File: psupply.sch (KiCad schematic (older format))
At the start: 23 parts, among them U401 LM7815_TO220, U402 LM7915_TO220

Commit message: The board shall now support single channel only.
Signed-off-by: Nenad Radulovic <nenad.radulovic@seavus.com>
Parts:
- removed C402: 10u, Capacitor_THT:CP_Radial_D5.0mm_P2.00mm, symbol CP1
- removed C406, C408: 470n, Capacitor_THT:C_Rect_L9.0mm_W3.6mm_P7.50mm_MKT, symbol C
- removed C407: 10n, Capacitor_THT:C_Rect_L9.0mm_W3.4mm_P7.50mm_MKT, symbol C
- removed C410: 10m, Capacitor_THT:CP_Radial_D35.0mm_P10.00mm_SnapIn, symbol CP1
- removed D401, D402: 1N4007, Diode_THT:D_DO-41_SOD81_P10.16mm_Horizontal, symbol 1N4007
- removed D403: GBU1510, Diode_THT:Diode_Bridge_Vishay_GBU, symbol GBU4A
- removed R405: 1, Resistor_THT:R_Axial_DIN0309_L9.0mm_D3.2mm_P12.70mm_Horizontal, symbol R
- removed R406: 5k1, Resistor_THT:R_Axial_DIN0411_L9.9mm_D3.6mm_P12.70mm_Horizontal, symbol R
- removed U401: LM7815_TO220, TO_SOT_Packages_THT:TO-220_Vertical, symbol LM7815_TO220
- removed U402: LM7915_TO220, TO_SOT_Packages_THT:TO-220_Vertical, symbol LM7915_TO220
- added Q401: PN2222A, Package_TO_SOT_THT:TO-92_Inline_Narrow_Oval, symbol PN2222A
- C401: renamed from C409; value 10m -> 4m7; footprint Capacitor_THT:CP_Radial_D35.0mm_P10.00mm_SnapIn -> Capacitor_THT:CP_Radial_D25.0mm_P10.00mm_SnapIn; Manufacturer Multicomp:MCKLZ063M103P51Y -> EPCOS:B41252B7478M000; Vendor Farnell:2610649 -> Farnell:2750103; Voltage 50V -> 35V
- C402: renamed from C401; Manufacturer (none) -> Rybicon:35YXJ1000M12.5X20; Vendor (none) -> Farnell:2346262
- C403: value 1m -> 4m7; footprint Capacitor_THT:CP_Radial_D12.5mm_P5.00mm -> Capacitor_THT:CP_Radial_D25.0mm_P10.00mm_SnapIn; Manufacturer (none) -> EPCOS:B41252B7478M000; Vendor (none) -> Farnell:2750103
- C404: value 10u -> 1m; footprint Capacitor_THT:CP_Radial_D5.0mm_P2.00mm -> Capacitor_THT:CP_Radial_D12.5mm_P5.00mm; Manufacturer (none) -> Rybicon:35YXJ1000M12.5X20; Vendor (none) -> Farnell:2346262
- C405: value 10n -> 100n; footprint Capacitor_THT:C_Rect_L13.0mm_W4.0mm_P10.00mm_FKS3_FKP3_MKS4 -> Capacitor_SMD:C_1206_3216Metric_Pad1.24x1.80mm_HandSolder; Manufacturer Epcos:B32921C3103M000 -> Multicomp:MCSH31B104K101CT; Type X2 -> X7R; Vendor Farnell:1200827 -> Farnell:1856606; Voltage 305V -> 100V
- R401, R402: value 47 -> 1; Manufacturer (none) -> NEOHM-TE:ROX1SJ47R; Type C -> MO; Vendor (none) -> Farnell:1738569
- R403: value 1 -> 10; footprint Resistor_THT:R_Axial_DIN0309_L9.0mm_D3.2mm_P12.70mm_Horizontal -> Resistor_THT:R_Axial_DIN0411_L9.9mm_D3.6mm_P12.70mm_Horizontal; Manufacturer (none) -> NEOHM-TE:ROX1SJ47R; Power 1/4 -> 1/1; Type C -> MO; Vendor (none) -> Farnell:1738569
- R404: value 5k1 -> 1k; footprint Resistor_THT:R_Axial_DIN0411_L9.9mm_D3.6mm_P12.70mm_Horizontal -> Resistor_SMD:R_1206_3216Metric_Pad1.24x1.80mm_HandSolder; Power 1/1 -> (none); Type C -> (none)
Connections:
- net labels added: muten, mutep, outp, ps_ctrl_gnd, ps_ctrl_op, ps_ctrl_s_outp, ps_ctrl_s_ovrld, ps_ctrl_vdd12, ps_gnd, ps_prevcc, ps_prevee, ps_vcc, ps_vee, sgnd, spkgnd
- net labels removed: earth, m1, m2, trp1, trp2, trs_a, trs_b, trs_common
- wire segments 61 -> 42
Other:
- moved on the sheet: C401, RV401, RV402

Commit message: Switched to Kicad 5.0
Signed-off-by: Nenad Radulovic <nenad.b.radulovic@gmail.com>
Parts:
- removed C402, C404: 1m, Capacitor_THT:CP_Radial_D12.5mm_P5.00mm, symbol CP1
- removed C405: 100n, Capacitor_SMD:C_1206_3216Metric_Pad1.24x1.80mm_HandSolder, symbol C
- removed Q401: PN2222A, Package_TO_SOT_THT:TO-92_Inline_Narrow_Oval, symbol PN2222A
- removed R401, R402: 1, Resistor_THT:R_Axial_DIN0411_L9.9mm_D3.6mm_P12.70mm_Horizontal, symbol R
- removed R403: 10, Resistor_THT:R_Axial_DIN0411_L9.9mm_D3.6mm_P12.70mm_Horizontal, symbol R
- removed R404: 1k, Resistor_SMD:R_1206_3216Metric_Pad1.24x1.80mm_HandSolder, symbol R
- removed RV401, RV402: Varistor, Resistor_THT:R_Axial_DIN0414_L11.9mm_D4.5mm_P15.24mm_Horizontal, symbol Varistor
- C10: renamed from C401; symbol CP1 -> Device:CP1
- C11: renamed from C403; symbol CP1 -> Device:CP1

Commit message: Updated regarding v5.0
Still updateing regarding transition to v5.0
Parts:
- C10, C11: footprint Capacitor_THT:CP_Radial_D25.0mm_P10.00mm_SnapIn -> Capacitor_THT:CP_Radial_D22.0mm_P10.00mm_SnapIn; Manufacturer EPCOS:B41252B7478M000 -> EPCOS:B41252A7478M000; Vendor Farnell:2750103 -> Farnell:2468294
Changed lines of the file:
@@
 F 0 "C10" H 4525 1450 50  0000 L CNN
 F 1 "4m7" H 4525 1250 50  0000 L CNN
-F 2 "Capacitor_THT:CP_Radial_D25.0mm_P10.00mm_SnapIn" H 4500 1350 50  0001 C CNN
-F 3 "http://www.farnell.com/datasheets/2280821.pdf" H 4500 1350 50  0001 C CNN
+F 2 "Capacitor_THT:CP_Radial_D22.0mm_P10.00mm_SnapIn" H 4500 1350 50  0001 C CNN
+F 3 "http://www.farnell.com/datasheets/2130719.pdf" H 4500 1350 50  0001 C CNN
 F 4 "35V" H 4600 1150 60  0000 C CNN "Voltage"
-F 5 "Farnell:2750103" H 4500 1350 60  0001 C CNN "Vendor"
-F 6 "EPCOS:B41252B7478M000" H 4500 1350 60  0001 C CNN "Manufacturer"
+F 5 "Farnell:2468294" H 4500 1350 60  0001 C CNN "Vendor"
+F 6 "EPCOS:B41252A7478M000" H 4500 1350 60  0001 C CNN "Manufacturer"
 	1    4500 1350
 	1    0    0    -1
 $EndComp
 $Comp
-L minima-rescue:GNDPWR #PWR013
+L power:GNDPWR #PWR013
 U 1 1 5AC0AAC9
 P 4400 1600
@@
 ps_gnd
 $Comp
-L minima-rescue:GNDPWR #PWR012
+L power:GNDPWR #PWR012
 U 1 1 5ADE314C
 P 3300 1600
@@
 F 3 "" H 3000 1000 50  0001 C CNN
 	1    3000 1000
-	1    0    0    -1
-$EndComp
-$Comp
-L Device:CP1 C11
-U 1 1 5AE75EE3
-P 4500 1850
-F 0 "C11" H 4525 1950 50  0000 L CNN
-F 1 "4m7" H 4525 1750 50  0000 L CNN
-F 2 "Capacitor_THT:CP_Radial_D25.0mm_P10.00mm_SnapIn" H 4500 1850 50  0001 C CNN
-F 3 "http://www.farnell.com/datasheets/2280821.pdf" H 4500 1850 50  0001 C CNN
-F 4 "35V" H 4600 1650 60  0000 C CNN "Voltage"
-F 5 "Farnell:2750103" H 4500 1850 60  0001 C CNN "Vendor"
-F 6 "EPCOS:B41252B7478M000" H 4500 1850 60  0001 C CNN "Manufacturer"
-	1    4500 1850
 	1    0    0    -1
 $EndComp
@@
 Wire Wire Line
 	3300 1100 3300 1000
+$Comp
+L Device:CP1 C11
+U 1 1 5B60A435
+P 4500 1850
+F 0 "C11" H 4525 1950 50  0000 L CNN
+F 1 "4m7" H 4525 1750 50  0000 L CNN
+F 2 "Capacitor_THT:CP_Radial_D22.0mm_P10.00mm_SnapIn" H 4500 1850 50  0001 C CNN
+F 3 "http://www.farnell.com/datasheets/2130719.pdf" H 4500 1850 50  0001 C CNN
+F 4 "35V" H 4600 1650 60  0000 C CNN "Voltage"
+F 5 "Farnell:2468294" H 4500 1850 60  0001 C CNN "Vendor"
+F 6 "EPCOS:B41252A7478M000" H 4500 1850 60  0001 C CNN "Manufacturer"
+	1    4500 1850
+	1    0    0    -1
+$EndComp
 $EndSCHEMATC

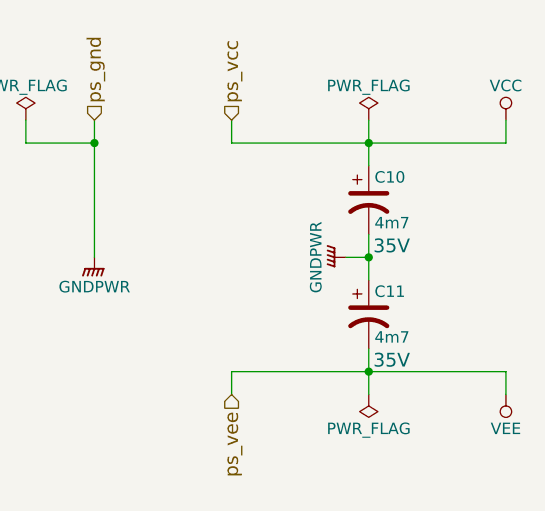
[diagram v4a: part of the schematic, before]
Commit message: Releasing version with distant psu caps.
Signed-off-by: Nenad Radulovic <nenad.b.radulovic@gmail.com>
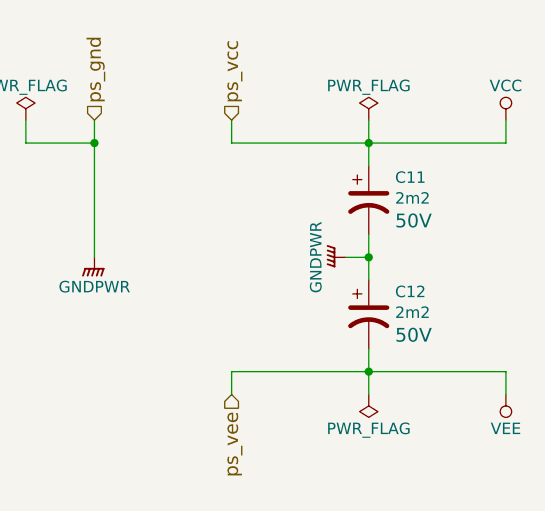
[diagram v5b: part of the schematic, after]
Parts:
- removed C11: 4m7, Capacitor_THT:CP_Radial_D22.0mm_P10.00mm_SnapIn, symbol Device:CP1
- added C12: 2m2, Capacitor_THT:CP_Radial_D16.0mm_P7.50mm, symbol Device:CP1
- C11: renamed from C10; value 4m7 -> 2m2; footprint Capacitor_THT:CP_Radial_D22.0mm_P10.00mm_SnapIn -> Capacitor_THT:CP_Radial_D16.0mm_P7.50mm; Manufacturer EPCOS:B41252A7478M000 -> Rubycon:50YXJ2200M16X35.5; Vendor Farnell:2468294 -> Farnell:2346272; Voltage 35V -> 50V
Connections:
- net GNDPWR: now also C12.1
- net VEE: now also C12.2
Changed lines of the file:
@@
 $EndDescr
 $Comp
-L Device:CP1 C10
+L Device:CP1 C11
 U 1 1 5AC0A8E9
 P 4500 1350
-F 0 "C10" H 4525 1450 50  0000 L CNN
-F 1 "4m7" H 4525 1250 50  0000 L CNN
-F 2 "Capacitor_THT:CP_Radial_D22.0mm_P10.00mm_SnapIn" H 4500 1350 50  0001 C CNN
-F 3 "http://www.farnell.com/datasheets/2130719.pdf" H 4500 1350 50  0001 C CNN
-F 4 "35V" H 4600 1150 60  0000 C CNN "Voltage"
-F 5 "Farnell:2468294" H 4500 1350 60  0001 C CNN "Vendor"
-F 6 "EPCOS:B41252A7478M000" H 4500 1350 60  0001 C CNN "Manufacturer"
+F 0 "C11" H 4615 1449 50  0000 L CNN
+F 1 "2m2" H 4615 1358 50  0000 L CNN
+F 2 "Capacitor_THT:CP_Radial_D16.0mm_P7.50mm" H 4500 1350 50  0001 C CNN
+F 3 "http://www.farnell.com/datasheets/2321616.pdf" H 4500 1350 50  0001 C CNN
+F 4 "50V" H 4615 1259 60  0000 L CNN "Voltage"
+F 5 "Farnell:2346272" H 4500 1350 60  0001 C CNN "Vendor"
+F 6 "Rubycon:50YXJ2200M16X35.5 " H 4500 1350 60  0001 C CNN "Manufacturer"
 	1    4500 1350
 	1    0    0    -1
 $EndComp
 $Comp
-L power:GNDPWR #PWR012
+L power:GNDPWR #PWR014
 U 1 1 5AC0AAC9
 P 4400 1600
-F 0 "#PWR012" H 4400 1400 50  0001 C CNN
+F 0 "#PWR014" H 4400 1400 50  0001 C CNN
 F 1 "GNDPWR" H 4400 1470 50  0000 C CNN
 F 2 "" H 4400 1550 50  0001 C CNN
@@
 $EndComp
 $Comp
-L power:VCC #PWR013
+L power:VCC #PWR012
 U 1 1 5AC0C44A
 P 5100 1000
-F 0 "#PWR013" H 5100 850 50  0001 C CNN
+F 0 "#PWR012" H 5100 850 50  0001 C CNN
 F 1 "VCC" H 5100 1150 50  0000 C CNN
 F 2 "" H 5100 1000 50  0001 C CNN
@@
 $EndComp
 $Comp
-L power:VEE #PWR014
+L power:VEE #PWR015
 U 1 1 5AC0C478
 P 5100 2200
-F 0 "#PWR014" H 5100 2050 50  0001 C CNN
+F 0 "#PWR015" H 5100 2050 50  0001 C CNN
 F 1 "VEE" H 5100 2350 50  0000 C CNN
 F 2 "" H 5100 2200 50  0001 C CNN
@@
 ps_gnd
 $Comp
-L power:GNDPWR #PWR011
+L power:GNDPWR #PWR013
 U 1 1 5ADE314C
 P 3300 1600
-F 0 "#PWR011" H 3300 1400 50  0001 C CNN
+F 0 "#PWR013" H 3300 1400 50  0001 C CNN
 F 1 "GNDPWR" H 3300 1470 50  0000 C CNN
 F 2 "" H 3300 1550 50  0001 C CNN
@@
 	3300 1100 3300 1000
 $Comp
-L Device:CP1 C11
-U 1 1 5B60A435
+L Device:CP1 C12
+U 1 1 5B66EE15
 P 4500 1850
-F 0 "C11" H 4525 1950 50  0000 L CNN
-F 1 "4m7" H 4525 1750 50  0000 L CNN
-F 2 "Capacitor_THT:CP_Radial_D22.0mm_P10.00mm_SnapIn" H 4500 1850 50  0001 C CNN
-F 3 "http://www.farnell.com/datasheets/2130719.pdf" H 4500 1850 50  0001 C CNN
-F 4 "35V" H 4600 1650 60  0000 C CNN "Voltage"
-F 5 "Farnell:2468294" H 4500 1850 60  0001 C CNN "Vendor"
-F 6 "EPCOS:B41252A7478M000" H 4500 1850 60  0001 C CNN "Manufacturer"
+F 0 "C12" H 4615 1949 50  0000 L CNN
+F 1 "2m2" H 4615 1858 50  0000 L CNN
+F 2 "Capacitor_THT:CP_Radial_D16.0mm_P7.50mm" H 4500 1850 50  0001 C CNN
+F 3 "http://www.farnell.com/datasheets/2321616.pdf" H 4500 1850 50  0001 C CNN
+F 4 "50V" H 4615 1759 60  0000 L CNN "Voltage"
+F 5 "Farnell:2346272" H 4500 1850 60  0001 C CNN "Vendor"
+F 6 "Rubycon:50YXJ2200M16X35.5 " H 4500 1850 60  0001 C CNN "Manufacturer"
 	1    4500 1850
 	1    0    0    -1
